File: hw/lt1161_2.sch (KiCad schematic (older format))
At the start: 6 parts, among them U901 MOSFET_DRIVER_LT1161, U902 MOSFET_IPG20N04S4L11ATMA1, U903 MOSFET_IPG20N04S4L11ATMA1

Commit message: analog shortcircuit protection added to LT1161
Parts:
- added C903, C904, C905, C906: 100nF, kemet:0603, symbol 100nF
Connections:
- wire segments 68 -> 79

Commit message: tag 3.0.0 schematic drawing started
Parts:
- renumbered C903 to C901, C904 to C902, C905 to C903, C906 to C904, C901 to C905, C902 to C906
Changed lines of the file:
@@
 $EndSheet
 $Comp
-L GND #PWR902
+L GND #PWR035
 U 1 1 594D8B81
 P 3400 4650
-F 0 "#PWR902" H 3400 4400 50  0001 C CNN
+F 0 "#PWR035" H 3400 4400 50  0001 C CNN
 F 1 "GND" H 3405 4477 50  0000 C CNN
 F 2 "" H 3400 4650 50  0000 C CNN
@@
 AR Path="/594D8B84" Ref="C?"  Part="1"
 AR Path="/58BE52C9/594D8B84" Ref="C?"  Part="1"
-AR Path="/58C7B0A8/594D8B84" Ref="C901"  Part="1"
-F 0 "C901" H 5250 3599 45  0000 C CNN
+AR Path="/58C7B0A8/594D8B84" Ref="C905"  Part="1"
+F 0 "C905" H 5250 3599 45  0000 C CNN
 F 1 "100nF" H 5250 3515 45  0000 C CNN
 F 2 "kemet:0603" H 5230 3550 20  0001 C CNN
@@
 AR Path="/58BE8EBA" Ref="C?"  Part="1"
 AR Path="/58BE52C9/58BE8EBA" Ref="C?"  Part="1"
-AR Path="/58C7B0A8/58BE8EBA" Ref="C902"  Part="1"
-F 0 "C902" H 5250 4749 45  0000 C CNN
+AR Path="/58C7B0A8/58BE8EBA" Ref="C906"  Part="1"
+F 0 "C906" H 5250 4749 45  0000 C CNN
 F 1 "100nF" H 5250 4665 45  0000 C CNN
 F 2 "kemet:0603" H 5230 4700 20  0001 C CNN
@@
 $EndComp
 $Comp
-L GND #PWR903
+L GND #PWR036
 U 1 1 594D8B86
 P 5400 4650
-F 0 "#PWR903" H 5400 4400 50  0001 C CNN
+F 0 "#PWR036" H 5400 4400 50  0001 C CNN
 F 1 "GND" H 5405 4477 50  0000 C CNN
 F 2 "" H 5400 4650 50  0000 C CNN
@@
 Connection ~ 2050 3650
 $Comp
-L GND #PWR901
+L GND #PWR037
 U 1 1 594D8B8C
 P 2050 4950
-F 0 "#PWR901" H 2050 4700 50  0001 C CNN
+F 0 "#PWR037" H 2050 4700 50  0001 C CNN
 F 1 "GND" H 2055 4777 50  0000 C CNN
 F 2 "" H 2050 4950 50  0000 C CNN
@@
 	4050 2450 6750 2450
 $Comp
-L 100nF C903
+L 100nF C901
 U 1 1 59AE9086
 P 3650 3550
-F 0 "C903" H 3700 3749 45  0000 C CNN
+F 0 "C901" H 3700 3749 45  0000 C CNN
 F 1 "100nF" H 3700 3665 45  0000 C CNN
 F 2 "kemet:0603" H 3680 3700 20  0001 C CNN
@@
 $EndComp
 $Comp
-L 100nF C904
+L 100nF C902
 U 1 1 59AE918D
 P 3650 3800
-F 0 "C904" H 3700 3999 45  0000 C CNN
+F 0 "C902" H 3700 3999 45  0000 C CNN
 F 1 "100nF" H 3700 3915 45  0000 C CNN
 F 2 "kemet:0603" H 3680 3950 20  0001 C CNN
@@
 $EndComp
 $Comp
-L 100nF C905
+L 100nF C903
 U 1 1 59AE9214
 P 3650 4050
-F 0 "C905" H 3700 4249 45  0000 C CNN
+F 0 "C903" H 3700 4249 45  0000 C CNN
 F 1 "100nF" H 3700 4165 45  0000 C CNN
 F 2 "kemet:0603" H 3680 4200 20  0001 C CNN
@@
 $EndComp
 $Comp
-L 100nF C906
+L 100nF C904
 U 1 1 59AE92A2
 P 3650 4300
-F 0 "C906" H 3700 4499 45  0000 C CNN
+F 0 "C904" H 3700 4499 45  0000 C CNN
 F 1 "100nF" H 3700 4415 45  0000 C CNN
 F 2 "kemet:0603" H 3680 4450 20  0001 C CNN

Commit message: added binary and build files to gitignore
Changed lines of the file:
@@
 $EndSheet
 $Comp
-L GND #PWR035
+L GND #PWR034
 U 1 1 594D8B81
 P 3400 4650
-F 0 "#PWR035" H 3400 4400 50  0001 C CNN
+F 0 "#PWR034" H 3400 4400 50  0001 C CNN
 F 1 "GND" H 3405 4477 50  0000 C CNN
 F 2 "" H 3400 4650 50  0000 C CNN
@@
 U 58BE8E88
 F0 "sheet58BE8E47" 60
-F1 "currentSense.sch" 60
+F1 "currentSense2.sch" 60
 F2 "SENSE+" I R 7550 4200 60
 F3 "SENSE-" I R 7550 4350 60
@@
 $EndComp
 $Comp
-L GND #PWR036
+L GND #PWR035
 U 1 1 594D8B86
 P 5400 4650
-F 0 "#PWR036" H 5400 4400 50  0001 C CNN
+F 0 "#PWR035" H 5400 4400 50  0001 C CNN
 F 1 "GND" H 5405 4477 50  0000 C CNN
 F 2 "" H 5400 4650 50  0000 C CNN
@@
 Connection ~ 2050 3650
 $Comp
-L GND #PWR037
+L GND #PWR036
 U 1 1 594D8B8C
 P 2050 4950
-F 0 "#PWR037" H 2050 4700 50  0001 C CNN
+F 0 "#PWR036" H 2050 4700 50  0001 C CNN
 F 1 "GND" H 2055 4777 50  0000 C CNN
 F 2 "" H 2050 4950 50  0000 C CNN

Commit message: 3.0.0 ready to order
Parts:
- removed C901, C902, C903, C904, C905, C906: 100nF, kemet:0603, symbol 100nF
- removed R901: R_ARRAY4_1K, usevolt:0603_array4, symbol R_ARRAY4_1K
- removed U901: MOSFET_DRIVER_LT1161, usevolt:SO20, symbol MOSFET_DRIVER_LT1161
- removed U902, U903: MOSFET_IPG20N04S4L11ATMA1, usevolt:PG-TDSON-8-4, symbol MOSFET_IPG20N04S4L11ATMA1
- added R601, R602: 390, yageo:0603, symbol 390
- added R603, R604: 560, yageo:0603, symbol 560
- added U601: VND5050AJTR-E, usevolt:PowerSSO-12, symbol VND5050AJTR-E
- added U602, U603: BTS6133D, usevolt:DPAK-5, symbol BTS6133D
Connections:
- wire segments 79 -> 42
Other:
- note removed: "OUT4 current sensing specsed for 4 Amps"

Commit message: 4.1.0 hw created, not yet ordered
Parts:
- added R605, R606, R607, R608: 1K, yageo:0603, symbol 1K
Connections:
- net GND: now also R605.1 (R1), R606.1 (R1), R607.1 (R1), R608.1 (R1)
- net IN1: now also R605.2 (R2)
- net IN2: now also R606.2 (R2)
- net IN3: now also R607.2 (R2)
- net IN4: now also R608.2 (R2)
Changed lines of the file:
@@
 Text HLabel 5800 4400 2    60   Output ~ 0
 OUT4
-Text HLabel 3950 2150 0    60   Input ~ 0
+Text HLabel 1900 2150 0    60   Input ~ 0
 IN1
-Text HLabel 3950 2850 0    60   Input ~ 0
+Text HLabel 1900 2850 0    60   Input ~ 0
 IN2
-Text HLabel 3500 3800 0    60   Input ~ 0
+Text HLabel 1900 3800 0    60   Input ~ 0
 IN3
-Text HLabel 3500 4000 0    60   Input ~ 0
+Text HLabel 1900 4000 0    60   Input ~ 0
 IN4
 Text HLabel 5450 2400 2    60   Output ~ 0
@@
 Text HLabel 5450 3100 2    60   Output ~ 0
 SENSE2
-Text HLabel 3200 3700 0    60   Output ~ 0
+Text HLabel 3350 3700 0    60   Output ~ 0
 SENSE3
-Text HLabel 3200 4200 0    60   Output ~ 0
+Text HLabel 3350 4200 0    60   Output ~ 0
 SENSE4
 $Comp
@@
 $EndComp
 $Comp
-L VDD #PWR025
+L VDD #PWR605
 U 1 1 59D808C7
 P 5250 3650
-F 0 "#PWR025" H 5250 3500 50  0001 C CNN
+F 0 "#PWR605" H 5250 3500 50  0001 C CNN
 F 1 "VDD" H 5267 3823 50  0000 C CNN
 F 2 "" H 5250 3650 50  0000 C CNN
@@
 Connection ~ 5250 4400
 Wire Wire Line
-	3500 3800 4300 3800
-Wire Wire Line
-	4300 4000 3500 4000
-$Comp
-L GND #PWR026
+	1900 3800 4300 3800
+Wire Wire Line
+	1900 4000 4300 4000
+$Comp
+L GND #PWR602
 U 1 1 59D86DC2
 P 3600 4450
-F 0 "#PWR026" H 3600 4200 50  0001 C CNN
+F 0 "#PWR602" H 3600 4200 50  0001 C CNN
 F 1 "GND" H 3605 4277 50  0000 C CNN
 F 2 "" H 3600 4450 50  0000 C CNN
@@
 	4000 3900 4300 3900
 Wire Wire Line
-	3200 4200 4150 4200
+	3350 4200 4150 4200
 Wire Wire Line
 	4150 4200 4150 4100
@@
 	4150 3900 4150 3700
 Wire Wire Line
-	4150 3700 3200 3700
+	4150 3700 3350 3700
 Connection ~ 4150 3900
 $Comp
@@
 $EndComp
 $Comp
-L VDD #PWR027
+L VDD #PWR604
 U 1 1 59D89B9B
 P 4600 1950
-F 0 "#PWR027" H 4600 1800 50  0001 C CNN
+F 0 "#PWR604" H 4600 1800 50  0001 C CNN
 F 1 "VDD" H 4617 2123 50  0000 C CNN
 F 2 "" H 4600 1950 50  0000 C CNN
@@
 Connection ~ 4700 2950
 Wire Wire Line
-	3950 2850 4750 2850
-Wire Wire Line
-	4750 2150 3950 2150
-$Comp
-L GND #PWR028
+	1900 2850 4750 2850
+Wire Wire Line
+	1900 2150 4750 2150
+$Comp
+L GND #PWR603
 U 1 1 59D8A4D0
 P 4050 3100
-F 0 "#PWR028" H 4050 2850 50  0001 C CNN
+F 0 "#PWR603" H 4050 2850 50  0001 C CNN
 F 1 "GND" H 4055 2927 50  0000 C CNN
 F 2 "" H 4050 3100 50  0000 C CNN
@@
 	5550 2250 5550 2150
 Connection ~ 5550 2150
+Wire Wire Line
+	2250 4300 2100 4300
+Wire Wire Line
+	2100 4300 2100 3800
+Connection ~ 2100 3800
+Wire Wire Line
+	2250 4650 2000 4650
+Wire Wire Line
+	2000 4650 2000 4000
+Connection ~ 2000 4000
+Wire Wire Line
+	2250 3150 2100 3150
+Wire Wire Line
+	2100 3150 2100 2850
+Connection ~ 2100 2850
+Wire Wire Line
+	2250 2450 2100 2450
+Wire Wire Line
+	2100 2450 2100 2150
+Connection ~ 2100 2150
+$Comp
+L GND #PWR601
+U 1 1 5A024814
+P 2800 4750
+F 0 "#PWR601" H 2800 4500 50  0001 C CNN
+F 1 "GND" H 2805 4577 50  0000 C CNN
+F 2 "" H 2800 4750 50  0000 C CNN
+F 3 "" H 2800 4750 50  0000 C CNN
+	1    2800 4750
+	1    0    0    -1
+$EndComp
+Wire Wire Line
+	2800 2450 2800 4750
+Wire Wire Line
+	2800 4650 2550 4650
+Wire Wire Line
+	2800 4300 2550 4300
+Connection ~ 2800 4650
+Wire Wire Line
+	2800 3150 2550 3150
+Connection ~ 2800 4300
+Wire Wire Line
+	2800 2450 2550 2450
+Connection ~ 2800 3150
+$Comp
+L 1K R605
+U 1 1 5A02ED15
+P 2350 2450
+F 0 "R605" H 2400 2634 45  0000 C CNN
+F 1 "1K" H 2400 2550 45  0000 C CNN
+F 2 "yageo:0603" H 2380 2600 20  0001 C CNN
+F 3 "" H 2319 2489 60  0001 C CNN
+F 4 "" H 2719 2889 60  0001 C CNN "1st Source Part Number"
+F 5 "Digikey" H 2619 2789 60  0001 C CNN "1st Source"
+F 6 "RC0603FR-071KL" H 2519 2689 60  0001 C CNN "Manufacturer Part Number"
+F 7 "YAGEO" H 2419 2589 60  0001 C CNN "Manufacturer"
+	1    2350 2450
+	1    0    0    -1
+$EndComp
+$Comp
+L 1K R606
+U 1 1 5A02ED9F
+P 2350 3150
+F 0 "R606" H 2400 3334 45  0000 C CNN
+F 1 "1K" H 2400 3250 45  0000 C CNN
+F 2 "yageo:0603" H 2380 3300 20  0001 C CNN
+F 3 "" H 2319 3189 60  0001 C CNN
+F 4 "" H 2719 3589 60  0001 C CNN "1st Source Part Number"
+F 5 "Digikey" H 2619 3489 60  0001 C CNN "1st Source"
+F 6 "RC0603FR-071KL" H 2519 3389 60  0001 C CNN "Manufacturer Part Number"
+F 7 "YAGEO" H 2419 3289 60  0001 C CNN "Manufacturer"
+	1    2350 3150
+	1    0    0    -1
+$EndComp
+$Comp
+L 1K R607
+U 1 1 5A02EDEA
+P 2350 4300
+F 0 "R607" H 2400 4484 45  0000 C CNN
+F 1 "1K" H 2400 4400 45  0000 C CNN
+F 2 "yageo:0603" H 2380 4450 20  0001 C CNN
+F 3 "" H 2319 4339 60  0001 C CNN
+F 4 "" H 2719 4739 60  0001 C CNN "1st Source Part Number"
+F 5 "Digikey" H 2619 4639 60  0001 C CNN "1st Source"
+F 6 "RC0603FR-071KL" H 2519 4539 60  0001 C CNN "Manufacturer Part Number"
+F 7 "YAGEO" H 2419 4439 60  0001 C CNN "Manufacturer"
+	1    2350 4300
+	1    0    0    -1
+$EndComp
+$Comp
+L 1K R608
+U 1 1 5A02EE4E
+P 2350 4650
+F 0 "R608" H 2400 4834 45  0000 C CNN
+F 1 "1K" H 2400 4750 45  0000 C CNN
+F 2 "yageo:0603" H 2380 4800 20  0001 C CNN
+F 3 "" H 2319 4689 60  0001 C CNN
+F 4 "" H 2719 5089 60  0001 C CNN "1st Source Part Number"
+F 5 "Digikey" H 2619 4989 60  0001 C CNN "1st Source"
+F 6 "RC0603FR-071KL" H 2519 4889 60  0001 C CNN "Manufacturer Part Number"
+F 7 "YAGEO" H 2419 4789 60  0001 C CNN "Manufacturer"
+	1    2350 4650
+	1    0    0    -1
+$EndComp
 $EndSCHEMATC

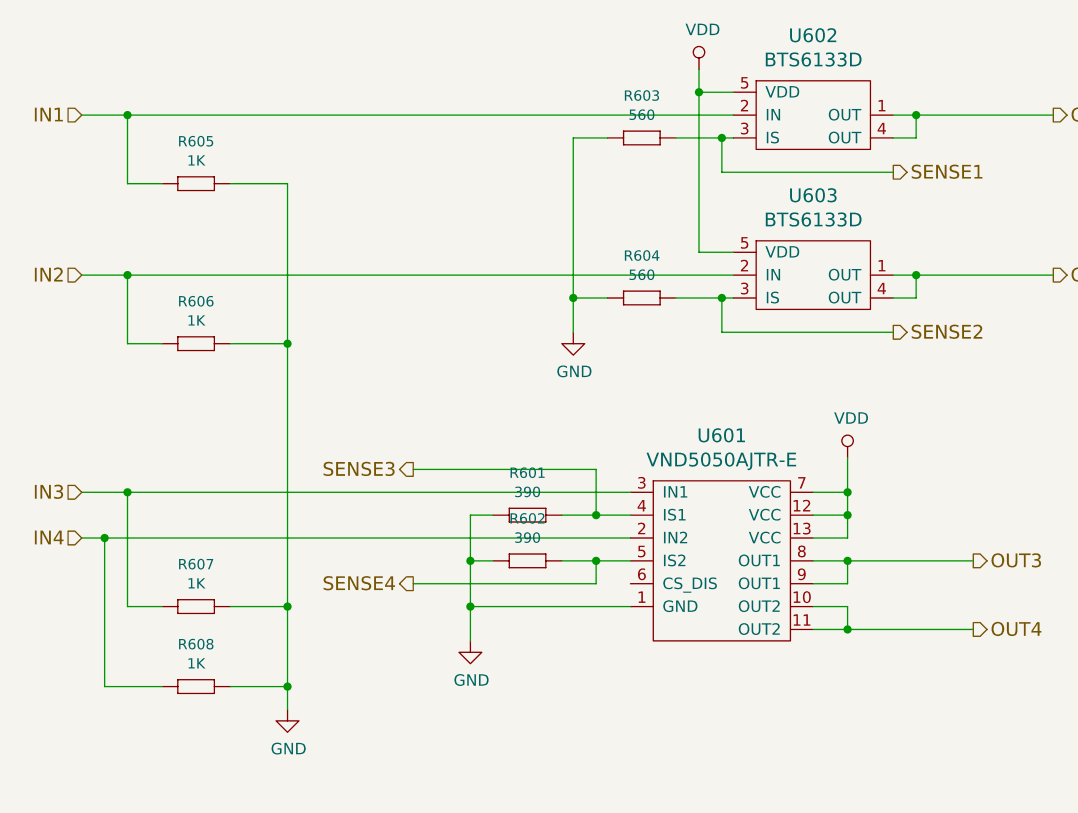
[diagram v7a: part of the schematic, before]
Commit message: 4.2.0 created, with working propo solenoid pump driver
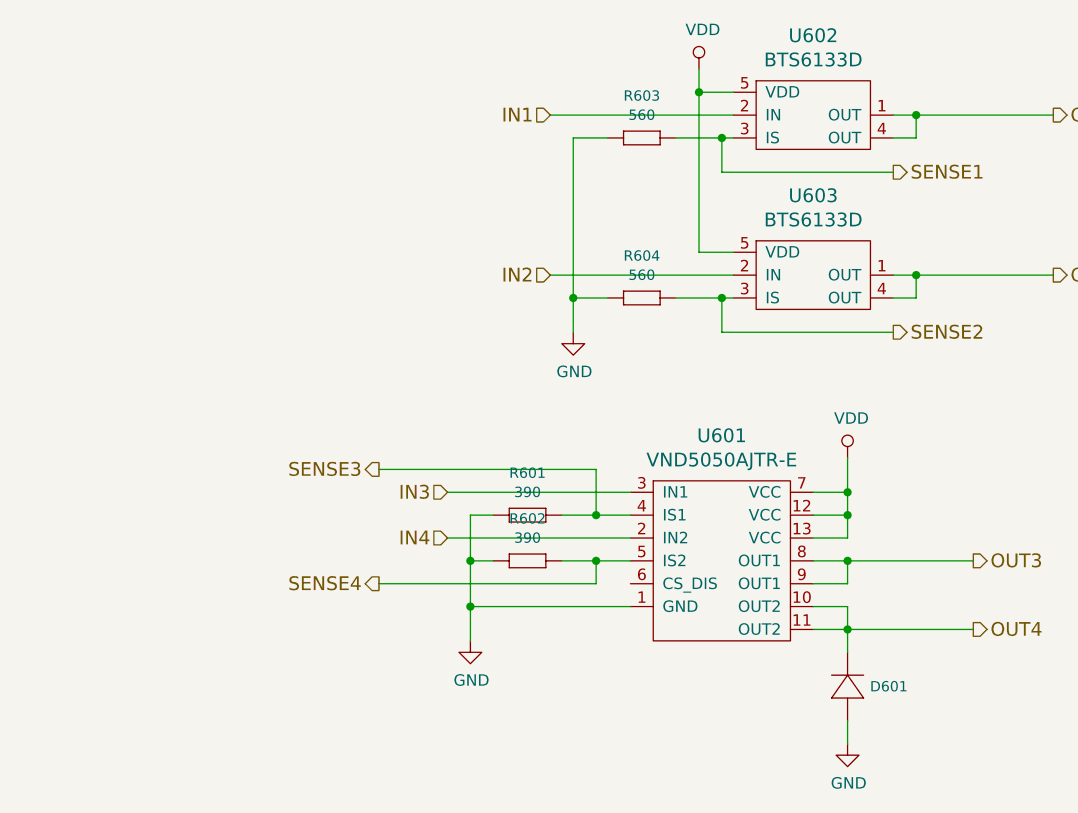
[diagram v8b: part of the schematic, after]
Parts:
- removed R605, R606, R607, R608: 1K, yageo:0603, symbol 1K
- added D601: DIODE_RS07J-GS18, usevolt:DO219AB, symbol DIODE_RS07J-GS18
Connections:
- net GND: now also D601.P$1 (P)
- net OUT4: now also D601.P$2 (N)
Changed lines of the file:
@@
 $Descr A4 11693 8268
 encoding utf-8
-Sheet 6 9
+Sheet 6 11
 Title ""
 Date ""
@@
 Text HLabel 5800 4400 2    60   Output ~ 0
 OUT4
-Text HLabel 1900 2150 0    60   Input ~ 0
+Text HLabel 3950 2150 0    60   Input ~ 0
 IN1
-Text HLabel 1900 2850 0    60   Input ~ 0
+Text HLabel 3950 2850 0    60   Input ~ 0
 IN2
-Text HLabel 1900 3800 0    60   Input ~ 0
+Text HLabel 3500 3800 0    60   Input ~ 0
 IN3
-Text HLabel 1900 4000 0    60   Input ~ 0
+Text HLabel 3500 4000 0    60   Input ~ 0
 IN4
 Text HLabel 5450 2400 2    60   Output ~ 0
@@
 Text HLabel 5450 3100 2    60   Output ~ 0
 SENSE2
-Text HLabel 3350 3700 0    60   Output ~ 0
+Text HLabel 3200 3700 0    60   Output ~ 0
 SENSE3
-Text HLabel 3350 4200 0    60   Output ~ 0
+Text HLabel 3200 4200 0    60   Output ~ 0
 SENSE4
 $Comp
@@
 $EndComp
 $Comp
-L VDD #PWR605
+L VDD #PWR604
 U 1 1 59D808C7
 P 5250 3650
-F 0 "#PWR605" H 5250 3500 50  0001 C CNN
+F 0 "#PWR604" H 5250 3500 50  0001 C CNN
 F 1 "VDD" H 5267 3823 50  0000 C CNN
 F 2 "" H 5250 3650 50  0000 C CNN
@@
 	5100 4300 5250 4300
 Wire Wire Line
-	5250 4300 5250 4400
+	5250 4300 5250 4500
 Connection ~ 5250 4400
 Wire Wire Line
-	1900 3800 4300 3800
-Wire Wire Line
-	1900 4000 4300 4000
-$Comp
-L GND #PWR602
+	3500 3800 4300 3800
+Wire Wire Line
+	4300 4000 3500 4000
+$Comp
+L GND #PWR601
 U 1 1 59D86DC2
 P 3600 4450
-F 0 "#PWR602" H 3600 4200 50  0001 C CNN
+F 0 "#PWR601" H 3600 4200 50  0001 C CNN
 F 1 "GND" H 3605 4277 50  0000 C CNN
 F 2 "" H 3600 4450 50  0000 C CNN
@@
 	4000 3900 4300 3900
 Wire Wire Line
-	3350 4200 4150 4200
+	3200 4200 4150 4200
 Wire Wire Line
 	4150 4200 4150 4100
@@
 	4150 3900 4150 3700
 Wire Wire Line
-	4150 3700 3350 3700
+	4150 3700 3200 3700
 Connection ~ 4150 3900
 $Comp
@@
 $EndComp
 $Comp
-L VDD #PWR604
+L VDD #PWR603
 U 1 1 59D89B9B
 P 4600 1950
-F 0 "#PWR604" H 4600 1800 50  0001 C CNN
+F 0 "#PWR603" H 4600 1800 50  0001 C CNN
 F 1 "VDD" H 4617 2123 50  0000 C CNN
 F 2 "" H 4600 1950 50  0000 C CNN
@@
 Connection ~ 4700 2950
 Wire Wire Line
-	1900 2850 4750 2850
-Wire Wire Line
-	1900 2150 4750 2150
-$Comp
-L GND #PWR603
+	3950 2850 4750 2850
+Wire Wire Line
+	4750 2150 3950 2150
+$Comp
+L GND #PWR602
 U 1 1 59D8A4D0
 P 4050 3100
-F 0 "#PWR603" H 4050 2850 50  0001 C CNN
+F 0 "#PWR602" H 4050 2850 50  0001 C CNN
 F 1 "GND" H 4055 2927 50  0000 C CNN
 F 2 "" H 4050 3100 50  0000 C CNN
@@
 	5550 2250 5550 2150
 Connection ~ 5550 2150
-Wire Wire Line
-	2250 4300 2100 4300
-Wire Wire Line
-	2100 4300 2100 3800
-Connection ~ 2100 3800
-Wire Wire Line
-	2250 4650 2000 4650
-Wire Wire Line
-	2000 4650 2000 4000
-Connection ~ 2000 4000
-Wire Wire Line
-	2250 3150 2100 3150
-Wire Wire Line
-	2100 3150 2100 2850
-Connection ~ 2100 2850
-Wire Wire Line
-	2250 2450 2100 2450
-Wire Wire Line
-	2100 2450 2100 2150
-Connection ~ 2100 2150
-$Comp
-L GND #PWR601
-U 1 1 5A024814
-P 2800 4750
-F 0 "#PWR601" H 2800 4500 50  0001 C CNN
-F 1 "GND" H 2805 4577 50  0000 C CNN
-F 2 "" H 2800 4750 50  0000 C CNN
-F 3 "" H 2800 4750 50  0000 C CNN
-	1    2800 4750
-	1    0    0    -1
-$EndComp
-Wire Wire Line
-	2800 2450 2800 4750
-Wire Wire Line
-	2800 4650 2550 4650
-Wire Wire Line
-	2800 4300 2550 4300
-Connection ~ 2800 4650
-Wire Wire Line
-	2800 3150 2550 3150
-Connection ~ 2800 4300
-Wire Wire Line
-	2800 2450 2550 2450
-Connection ~ 2800 3150
-$Comp
-L 1K R605
-U 1 1 5A02ED15
-P 2350 2450
-F 0 "R605" H 2400 2634 45  0000 C CNN
-F 1 "1K" H 2400 2550 45  0000 C CNN
-F 2 "yageo:0603" H 2380 2600 20  0001 C CNN
-F 3 "" H 2319 2489 60  0001 C CNN
-F 4 "" H 2719 2889 60  0001 C CNN "1st Source Part Number"
-F 5 "Digikey" H 2619 2789 60  0001 C CNN "1st Source"
-F 6 "RC0603FR-071KL" H 2519 2689 60  0001 C CNN "Manufacturer Part Number"
-F 7 "YAGEO" H 2419 2589 60  0001 C CNN "Manufacturer"
-	1    2350 2450
-	1    0    0    -1
-$EndComp
-$Comp
-L 1K R606
-U 1 1 5A02ED9F
-P 2350 3150
-F 0 "R606" H 2400 3334 45  0000 C CNN
-F 1 "1K" H 2400 3250 45  0000 C CNN
-F 2 "yageo:0603" H 2380 3300 20  0001 C CNN
-F 3 "" H 2319 3189 60  0001 C CNN
-F 4 "" H 2719 3589 60  0001 C CNN "1st Source Part Number"
-F 5 "Digikey" H 2619 3489 60  0001 C CNN "1st Source"
-F 6 "RC0603FR-071KL" H 2519 3389 60  0001 C CNN "Manufacturer Part Number"
-F 7 "YAGEO" H 2419 3289 60  0001 C CNN "Manufacturer"
-	1    2350 3150
-	1    0    0    -1
-$EndComp
-$Comp
-L 1K R607
-U 1 1 5A02EDEA
-P 2350 4300
-F 0 "R607" H 2400 4484 45  0000 C CNN
-F 1 "1K" H 2400 4400 45  0000 C CNN
-F 2 "yageo:0603" H 2380 4450 20  0001 C CNN
-F 3 "" H 2319 4339 60  0001 C CNN
-F 4 "" H 2719 4739 60  0001 C CNN "1st Source Part Number"
-F 5 "Digikey" H 2619 4639 60  0001 C CNN "1st Source"
-F 6 "RC0603FR-071KL" H 2519 4539 60  0001 C CNN "Manufacturer Part Number"
-F 7 "YAGEO" H 2419 4439 60  0001 C CNN "Manufacturer"
-	1    2350 4300
-	1    0    0    -1
-$EndComp
-$Comp
-L 1K R608
-U 1 1 5A02EE4E
-P 2350 4650
-F 0 "R608" H 2400 4834 45  0000 C CNN
-F 1 "1K" H 2400 4750 45  0000 C CNN
-F 2 "yageo:0603" H 2380 4800 20  0001 C CNN
-F 3 "" H 2319 4689 60  0001 C CNN
-F 4 "" H 2719 5089 60  0001 C CNN "1st Source Part Number"
-F 5 "Digikey" H 2619 4989 60  0001 C CNN "1st Source"
-F 6 "RC0603FR-071KL" H 2519 4889 60  0001 C CNN "Manufacturer Part Number"
-F 7 "YAGEO" H 2419 4789 60  0001 C CNN "Manufacturer"
-	1    2350 4650
-	1    0    0    -1
-$EndComp
+$Comp
+L DIODE_RS07J-GS18 D601
+U 1 1 5A102340
+P 5250 4600
+F 0 "D601" V 5200 4502 45  0000 R CNN
+F 1 "DIODE_RS07J-GS18" H 5270 4540 45  0001 L BNN
+F 2 "usevolt:DO219AB" H 5280 4750 20  0001 C CNN
+F 3 "http://www.vishay.com/docs/85742/rs07b.pdf" H 5270 4620 60  0001 C CNN
+F 4 "1864882" H 5870 5220 60  0001 C CNN "2nd Source Part Number"
+F 5 "Digi-Key" H 5570 4920 60  0001 C CNN "1st Source"
+F 6 "Farnell" H 5770 5120 60  0001 C CNN "2nd Source"
+F 7 "RS07J-GS18" H 5470 4820 60  0001 C CNN "Manufacturer Part Number"
+F 8 "RS07J-GS18-ND" H 5670 5020 60  0001 C CNN "1st Source Part Number"
+F 9 "Vishay Semiconductor Diodes Division" H 5370 4720 60  0001 C CNN "Manufacturer"
+	1    5250 4600
+	0    -1   -1   0
+$EndComp
+$Comp
+L GND #PWR605
+U 1 1 5A10241D
+P 5250 4900
+F 0 "#PWR605" H 5250 4650 50  0001 C CNN
+F 1 "GND" H 5255 4727 50  0000 C CNN
+F 2 "" H 5250 4900 50  0000 C CNN
+F 3 "" H 5250 4900 50  0000 C CNN
+	1    5250 4900
+	1    0    0    -1
+$EndComp
+Wire Wire Line
+	5250 4900 5250 4800
 $EndSCHEMATC
